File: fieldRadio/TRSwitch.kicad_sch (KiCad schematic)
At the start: 36 parts, among them Q1 MMBT3904, Q2 MMBT3904, Q3 PMV240SP, Q5 MMBT3904, Q6 PMV240SP, Q7 BSS123

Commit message: Clean Up
Schematic clean up in prep for layout
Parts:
- L1, L2, L3, L4: footprint Inductor_THT:L_Axial_L11.0mm_D4.5mm_P7.62mm_Vertical_Fastron_MECC -> Inductor_THT:L_Axial_L13.0mm_D4.5mm_P15.24mm_Horizontal_Fastron_HCCC
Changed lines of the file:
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@@
       (project "fieldRadio"
         (path "/a1d1b2b0-2f27-4dc0-94ba-bb0e02933617/07223125-3b0c-43ef-b5d7-ce26f2ddaddd"
-          (reference "C3") (unit 1)
+          (reference "C5") (unit 1)
         )
       )
@@
       (project "fieldRadio"
         (path "/a1d1b2b0-2f27-4dc0-94ba-bb0e02933617/07223125-3b0c-43ef-b5d7-ce26f2ddaddd"
-          (reference "C4") (unit 1)
+          (reference "C6") (unit 1)
         )
       )
@@
       (effects (font (size 1.27 1.27)) (justify right))
     )
-    (property "Footprint" "Inductor_THT:L_Axial_L11.0mm_D4.5mm_P7.62mm_Vertical_Fastron_MECC" (at 311.15 123.19 0)
+    (property "Footprint" "Inductor_THT:L_Axial_L13.0mm_D4.5mm_P15.24mm_Horizontal_Fastron_HCCC" (at 311.15 123.19 0)
       (effects (font (size 1.27 1.27)) hide)
     )
@@
       (project "fieldRadio"
         (path "/a1d1b2b0-2f27-4dc0-94ba-bb0e02933617/07223125-3b0c-43ef-b5d7-ce26f2ddaddd"
-          (reference "#PWR02") (unit 1)
+          (reference "#PWR09") (unit 1)
         )
       )
@@
       (project "fieldRadio"
         (path "/a1d1b2b0-2f27-4dc0-94ba-bb0e02933617/07223125-3b0c-43ef-b5d7-ce26f2ddaddd"
-          (reference "C6") (unit 1)
+          (reference "C8") (unit 1)
         )
       )
@@
       (project "fieldRadio"
         (path "/a1d1b2b0-2f27-4dc0-94ba-bb0e02933617/07223125-3b0c-43ef-b5d7-ce26f2ddaddd"
-          (reference "#PWR04") (unit 1)
+          (reference "#PWR011") (unit 1)
         )
       )
@@
       (project "fieldRadio"
         (path "/a1d1b2b0-2f27-4dc0-94ba-bb0e02933617/07223125-3b0c-43ef-b5d7-ce26f2ddaddd"
-          (reference "C2") (unit 1)
+          (reference "C4") (unit 1)
         )
       )
@@
       (effects (font (size 1.27 1.27)) (justify right))
     )
-    (property "Footprint" "Inductor_THT:L_Axial_L11.0mm_D4.5mm_P7.62mm_Vertical_Fastron_MECC" (at 299.72 100.33 0)
+    (property "Footprint" "Inductor_THT:L_Axial_L13.0mm_D4.5mm_P15.24mm_Horizontal_Fastron_HCCC" (at 299.72 100.33 0)
       (effects (font (size 1.27 1.27)) hide)
     )
@@
       (effects (font (size 1.27 1.27)) (justify right))
     )
-    (property "Footprint" "Inductor_THT:L_Axial_L11.0mm_D4.5mm_P7.62mm_Vertical_Fastron_MECC" (at 265.43 123.19 0)
+    (property "Footprint" "Inductor_THT:L_Axial_L13.0mm_D4.5mm_P15.24mm_Horizontal_Fastron_HCCC" (at 265.43 123.19 0)
       (effects (font (size 1.27 1.27)) hide)
     )
@@
       (project "fieldRadio"
         (path "/a1d1b2b0-2f27-4dc0-94ba-bb0e02933617/07223125-3b0c-43ef-b5d7-ce26f2ddaddd"
-          (reference "#PWR05") (unit 1)
+          (reference "#PWR012") (unit 1)
         )
       )
@@
       (project "fieldRadio"
         (path "/a1d1b2b0-2f27-4dc0-94ba-bb0e02933617/07223125-3b0c-43ef-b5d7-ce26f2ddaddd"
-          (reference "#PWR03") (unit 1)
+          (reference "#PWR010") (unit 1)
         )
       )
@@
       (project "fieldRadio"
         (path "/a1d1b2b0-2f27-4dc0-94ba-bb0e02933617/07223125-3b0c-43ef-b5d7-ce26f2ddaddd"
-          (reference "C1") (unit 1)
+          (reference "C3") (unit 1)
         )
       )
@@
       (project "fieldRadio"
         (path "/a1d1b2b0-2f27-4dc0-94ba-bb0e02933617/07223125-3b0c-43ef-b5d7-ce26f2ddaddd"
+          (reference "C9") (unit 1)
+        )
+      )
+    )
+  )
+  (symbol (lib_id "Device:D") (at 292.1 129.54 0) (unit 1)
+    (in_bom yes) (on_board yes) (dnp no) (fields_autoplaced)
+    (property "Reference" "D4" (at 292.1 123.19 0)
+      (effects (font (size 1.27 1.27)))
+    )
+    (property "Value" "1N914" (at 292.1 125.73 0)
+      (effects (font (size 1.27 1.27)))
+    )
+    (property "Footprint" "Diode_THT:D_DO-35_SOD27_P7.62mm_Horizontal" (at 292.1 129.54 0)
+      (effects (font (size 1.27 1.27)) hide)
+    )
+    (property "Datasheet" "~" (at 292.1 129.54 0)
+      (effects (font (size 1.27 1.27)) hide)
+    )
+    (property "Sim.Device" "D" (at 292.1 129.54 0)
+      (effects (font (size 1.27 1.27)) hide)
+    )
+    (property "Sim.Pins" "1=K 2=A" (at 292.1 129.54 0)
+      (effects (font (size 1.27 1.27)) hide)
+    )
+    (pin "1")
+    (pin "2")
+    (instances
+      (project ""
+        (path "/6f2c3d19-d4e9-42f1-a4a4-8f8c301ff52b"
+          (reference "D4") (unit 1)
+        )
+      )
+      (project "fieldRadio"
+        (path "/a1d1b2b0-2f27-4dc0-94ba-bb0e02933617/07223125-3b0c-43ef-b5d7-ce26f2ddaddd"
+          (reference "D4") (unit 1)
+        )
+      )
+    )
+  )
+  (symbol (lib_id "Device:L_Small") (at 196.85 129.54 90) (unit 1)
+    (in_bom yes) (on_board yes) (dnp no) (fields_autoplaced)
+    (property "Reference" "L1" (at 196.85 124.46 90)
+      (effects (font (size 1.27 1.27)))
+    )
+    (property "Value" "47uH" (at 196.85 127 90)
+      (effects (font (size 1.27 1.27)))
+    )
+    (property "Footprint" "Inductor_THT:L_Axial_L13.0mm_D4.5mm_P15.24mm_Horizontal_Fastron_HCCC" (at 196.85 129.54 0)
+      (effects (font (size 1.27 1.27)) hide)
+    )
+    (property "Datasheet" "~" (at 196.85 129.54 0)
+      (effects (font (size 1.27 1.27)) hide)
+    )
+    (pin "1")
+    (pin "2")
+    (instances
+      (project "fieldRadio"
+        (path "/a1d1b2b0-2f27-4dc0-94ba-bb0e02933617/07223125-3b0c-43ef-b5d7-ce26f2ddaddd"
+          (reference "L1") (unit 1)
+        )
+      )
+    )
+  )
+  (symbol (lib_id "Device:C_Small") (at 280.67 129.54 90) (unit 1)
+    (in_bom yes) (on_board yes) (dnp no)
+    (property "Reference" "C3" (at 278.13 130.81 90)
+      (effects (font (size 1.27 1.27)))
+    )
+    (property "Value" "15pF" (at 280.67 133.35 90)
+      (effects (font (size 1.27 1.27)))
+    )
+    (property "Footprint" "Capacitor_THT:C_Disc_D5.0mm_W2.5mm_P5.00mm" (at 280.67 129.54 0)
+      (effects (font (size 1.27 1.27)) hide)
+    )
+    (property "Datasheet" "~" (at 280.67 129.54 0)
+      (effects (font (size 1.27 1.27)) hide)
+    )
+    (pin "1")
+    (pin "2")
+    (instances
+      (project ""
+        (path "/6f2c3d19-d4e9-42f1-a4a4-8f8c301ff52b"
+          (reference "C3") (unit 1)
+        )
+      )
+      (project "fieldRadio"
+        (path "/a1d1b2b0-2f27-4dc0-94ba-bb0e02933617/07223125-3b0c-43ef-b5d7-ce26f2ddaddd"
           (reference "C7") (unit 1)
         )
       )
-    )
-  )
-  (symbol (lib_id "Device:D") (at 292.1 129.54 0) (unit 1)
-    (in_bom yes) (on_board yes) (dnp no) (fields_autoplaced)
-    (property "Reference" "D4" (at 292.1 123.19 0)
-      (effects (font (size 1.27 1.27)))
-    )
-    (property "Value" "1N914" (at 292.1 125.73 0)
-      (effects (font (size 1.27 1.27)))
-    )
-    (property "Footprint" "Diode_THT:D_DO-35_SOD27_P7.62mm_Horizontal" (at 292.1 129.54 0)
-      (effects (font (size 1.27 1.27)) hide)
-    )
-    (property "Datasheet" "~" (at 292.1 129.54 0)
-      (effects (font (size 1.27 1.27)) hide)
-    )
-    (property "Sim.Device" "D" (at 292.1 129.54 0)
-      (effects (font (size 1.27 1.27)) hide)
-    )
-    (property "Sim.Pins" "1=K 2=A" (at 292.1 129.54 0)
-      (effects (font (size 1.27 1.27)) hide)
-    )
-    (pin "1")
-    (pin "2")
-    (instances
-      (project ""
-        (path "/6f2c3d19-d4e9-42f1-a4a4-8f8c301ff52b"
-          (reference "D4") (unit 1)
-        )
-      )
-      (project "fieldRadio"
-        (path "/a1d1b2b0-2f27-4dc0-94ba-bb0e02933617/07223125-3b0c-43ef-b5d7-ce26f2ddaddd"
-          (reference "D4") (unit 1)
-        )
-      )
-    )
-  )
-  (symbol (lib_id "Device:L_Small") (at 196.85 129.54 90) (unit 1)
-    (in_bom yes) (on_board yes) (dnp no) (fields_autoplaced)
-    (property "Reference" "L1" (at 196.85 124.46 90)
-      (effects (font (size 1.27 1.27)))
-    )
-    (property "Value" "47uH" (at 196.85 127 90)
-      (effects (font (size 1.27 1.27)))
-    )
-    (property "Footprint" "Inductor_THT:L_Axial_L11.0mm_D4.5mm_P7.62mm_Vertical_Fastron_MECC" (at 196.85 129.54 0)
-      (effects (font (size 1.27 1.27)) hide)
-    )
-    (property "Datasheet" "~" (at 196.85 129.54 0)
-      (effects (font (size 1.27 1.27)) hide)
-    )
-    (pin "1")
-    (pin "2")
-    (instances
-      (project "fieldRadio"
-        (path "/a1d1b2b0-2f27-4dc0-94ba-bb0e02933617/07223125-3b0c-43ef-b5d7-ce26f2ddaddd"
-          (reference "L1") (unit 1)
-        )
-      )
-    )
-  )
-  (symbol (lib_id "Device:C_Small") (at 280.67 129.54 90) (unit 1)
-    (in_bom yes) (on_board yes) (dnp no)
-    (property "Reference" "C3" (at 278.13 130.81 90)
-      (effects (font (size 1.27 1.27)))
-    )
-    (property "Value" "15pF" (at 280.67 133.35 90)
-      (effects (font (size 1.27 1.27)))
-    )
-    (property "Footprint" "Capacitor_THT:C_Disc_D5.0mm_W2.5mm_P5.00mm" (at 280.67 129.54 0)
-      (effects (font (size 1.27 1.27)) hide)
-    )
-    (property "Datasheet" "~" (at 280.67 129.54 0)
-      (effects (font (size 1.27 1.27)) hide)
-    )
-    (pin "1")
-    (pin "2")
-    (instances
-      (project ""
-        (path "/6f2c3d19-d4e9-42f1-a4a4-8f8c301ff52b"
-          (reference "C3") (unit 1)
-        )
-      )
-      (project "fieldRadio"
-        (path "/a1d1b2b0-2f27-4dc0-94ba-bb0e02933617/07223125-3b0c-43ef-b5d7-ce26f2ddaddd"
-          (reference "C5") (unit 1)
-        )
-      )

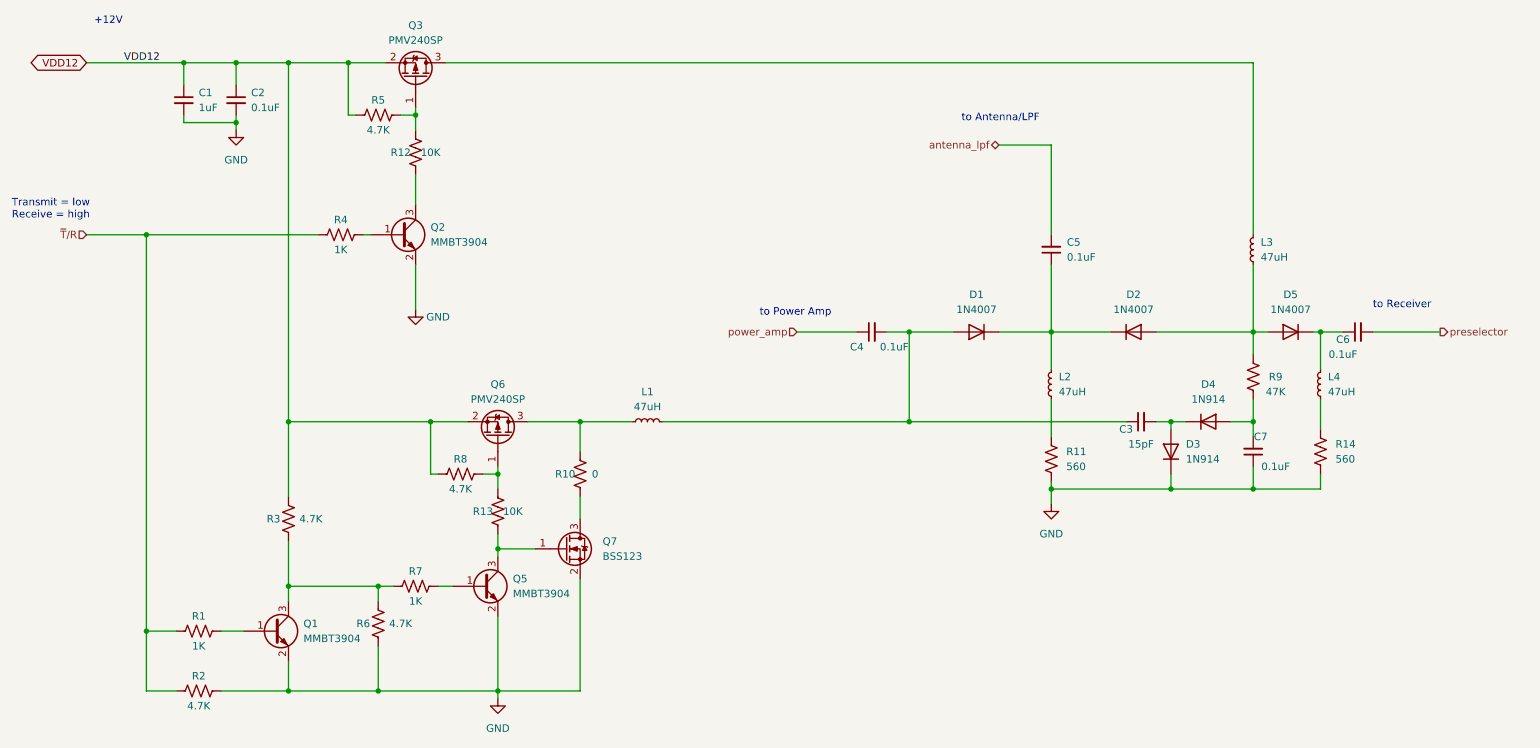
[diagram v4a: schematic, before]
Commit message: Placement of preselector and qsd
Finished placement of these two blocks
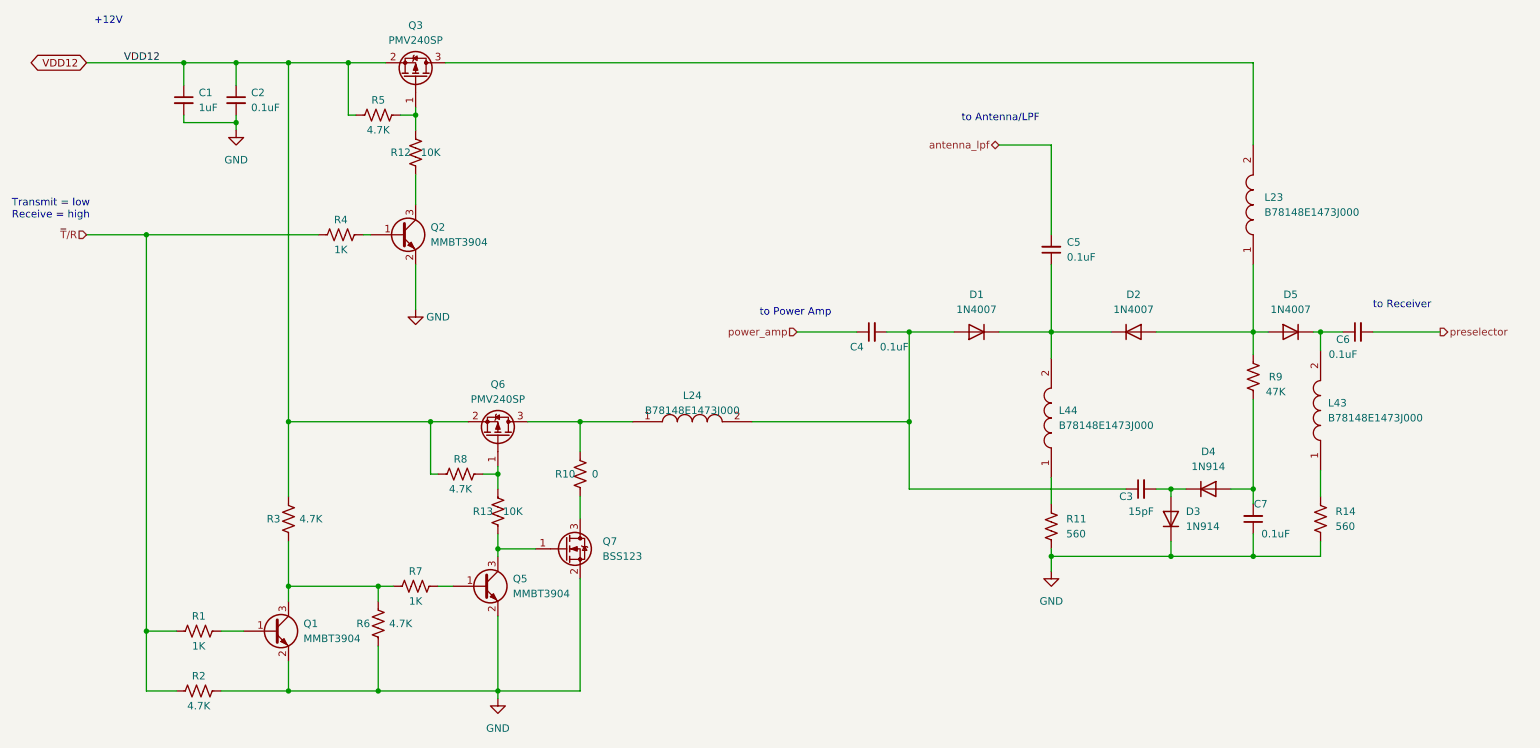
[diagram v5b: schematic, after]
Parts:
- removed L1, L2, L3, L4: 47uH, Inductor_THT:L_Axial_L13.0mm_D4.5mm_P15.24mm_Horizontal_Fastron_HCCC, symbol Device:L_Small
- added L23, L24, L43, L44: B78148E1473J000, B78148E, symbol SamacSys_Parts:B78148E1473J000
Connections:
- net at C5.1, D1.1 (K), D2.1 (K): now also L44.2
- net at D2.2 (A), D5.2 (A), R9.2: now also L23.1
- net at R11.1: now also L44.1
- net at C3.1, C4.2, D1.2 (A): now also L24.2
- net at R14.1: now also L43.1
- net at C6.1, D5.1 (K): now also L43.2
- net at Q3.3 (D): now also L23.2
- net at Q6.3 (D), R10.2: now also L24.1
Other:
- moved on the sheet: C3, C7, D3, D4, R11, R14

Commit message: First Clean DRC
first clean drc
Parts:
- R11, R14: footprint Resistor_THT:R_Axial_DIN0411_L9.9mm_D3.6mm_P15.24mm_Horizontal -> Resistor_THT:R_Axial_DIN0617_L17.0mm_D6.0mm_P20.32mm_Horizontal
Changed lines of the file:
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@@
   (symbol (lib_id "Device:R_US") (at 265.43 147.32 0) (unit 1)
     (in_bom yes) (on_board yes) (dnp no) (fields_autoplaced)
-    (property "Reference" "R11" (at 267.97 146.0499 0)
-      (effects (font (size 1.27 1.27)) (justify left))
-    )
-    (property "Value" "560" (at 267.97 148.5899 0)
-      (effects (font (size 1.27 1.27)) (justify left))
-    )
-    (property "Footprint" "Resistor_THT:R_Axial_DIN0411_L9.9mm_D3.6mm_P15.24mm_Horizontal" (at 266.446 147.574 90)
+    (property "Reference" "R11" (at 267.97 146.05 0)
+      (effects (font (size 1.27 1.27)) (justify left))
+    )
+    (property "Value" "560" (at 267.97 148.59 0)
+      (effects (font (size 1.27 1.27)) (justify left))
+    )
+    (property "Footprint" "Resistor_THT:R_Axial_DIN0617_L17.0mm_D6.0mm_P20.32mm_Horizontal" (at 266.446 147.574 90)
       (effects (font (size 1.27 1.27)) hide)
     )
@@
   (symbol (lib_id "Device:R_US") (at 311.15 146.05 0) (unit 1)
     (in_bom yes) (on_board yes) (dnp no) (fields_autoplaced)
-    (property "Reference" "R14" (at 313.69 144.7799 0)
-      (effects (font (size 1.27 1.27)) (justify left))
-    )
-    (property "Value" "560" (at 313.69 147.3199 0)
-      (effects (font (size 1.27 1.27)) (justify left))
-    )
-    (property "Footprint" "Resistor_THT:R_Axial_DIN0411_L9.9mm_D3.6mm_P15.24mm_Horizontal" (at 312.166 146.304 90)
-      (effects (font (size 1.27 1.27)) hide)
-    )
+    (property "Reference" "R14" (at 313.69 144.78 0)
+      (effects (font (size 1.27 1.27)) (justify left))
+    )
+    (property "Value" "560" (at 313.69 147.32 0)
+      (effects (font (size 1.27 1.27)) (justify left))
+    )
+    (property "Footprint" "Resistor_THT:R_Axial_DIN0617_L17.0mm_D6.0mm_P20.32mm_Horizontal" (at 312.166 146.304 90)
+      (effects (font (size 1.27 1.27)) hide)
+    )

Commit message: Added support for unused gpio
Also added option for external clock generator.
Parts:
- R11, R14: footprint Resistor_THT:R_Axial_DIN0617_L17.0mm_D6.0mm_P20.32mm_Horizontal -> Resistor_THT:R_Axial_DIN0207_L6.3mm_D2.5mm_P10.16mm_Horizontal
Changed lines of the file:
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@@
       (effects (font (size 1.27 1.27)) (justify left))
     )
-    (property "Footprint" "Resistor_THT:R_Axial_DIN0617_L17.0mm_D6.0mm_P20.32mm_Horizontal" (at 266.446 147.574 90)
+    (property "Footprint" "Resistor_THT:R_Axial_DIN0207_L6.3mm_D2.5mm_P10.16mm_Horizontal" (at 266.446 147.574 90)
       (effects (font (size 1.27 1.27)) hide)
     )
@@
       (effects (font (size 1.27 1.27)) (justify left))
     )
-    (property "Footprint" "Resistor_THT:R_Axial_DIN0617_L17.0mm_D6.0mm_P20.32mm_Horizontal" (at 312.166 146.304 90)
-      (effects (font (size 1.27 1.27)) hide)
-    )
+    (property "Footprint" "Resistor_THT:R_Axial_DIN0207_L6.3mm_D2.5mm_P10.16mm_Horizontal" (at 312.166 146.304 90)
+      (effects (font (size 1.27 1.27)) hide)
+    )
